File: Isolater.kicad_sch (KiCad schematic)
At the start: 15 parts, among them J29 Norcomp 172-009-243R021, J30 Pin Socket 0.1" 01x04, J32 Pin Socket 0.1" 01x04, U1 UCC12040DVE, U2 L7805CDT, U3 ISO1050DUB

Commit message: fix drc/erc errors
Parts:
- U1: footprint SO_0DVER_TEX -> footprints:SO_0DVER_TEX
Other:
- note removed: "TODO: verify dsub footprint"
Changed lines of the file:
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@@
     (stroke (width 0) (type default))
-  )
-  (text "TODO: verify dsub footprint\n" (at 15.24 24.13 0)
-    (effects (font (size 3 3) (thickness 0.8) bold (color 255 4 17 1)) (justify left bottom))
   )
   (text "Place close to connector" (at 154.94 95.25 0)
@@
       (effects (font (size 1.524 1.524)))
     )
-    (property "Footprint" "SO_0DVER_TEX" (at 207.01 40.64 0)
+    (property "Footprint" "footprints:SO_0DVER_TEX" (at 207.01 40.64 0)
       (effects (font (size 1.27 1.27) italic) hide)
     )

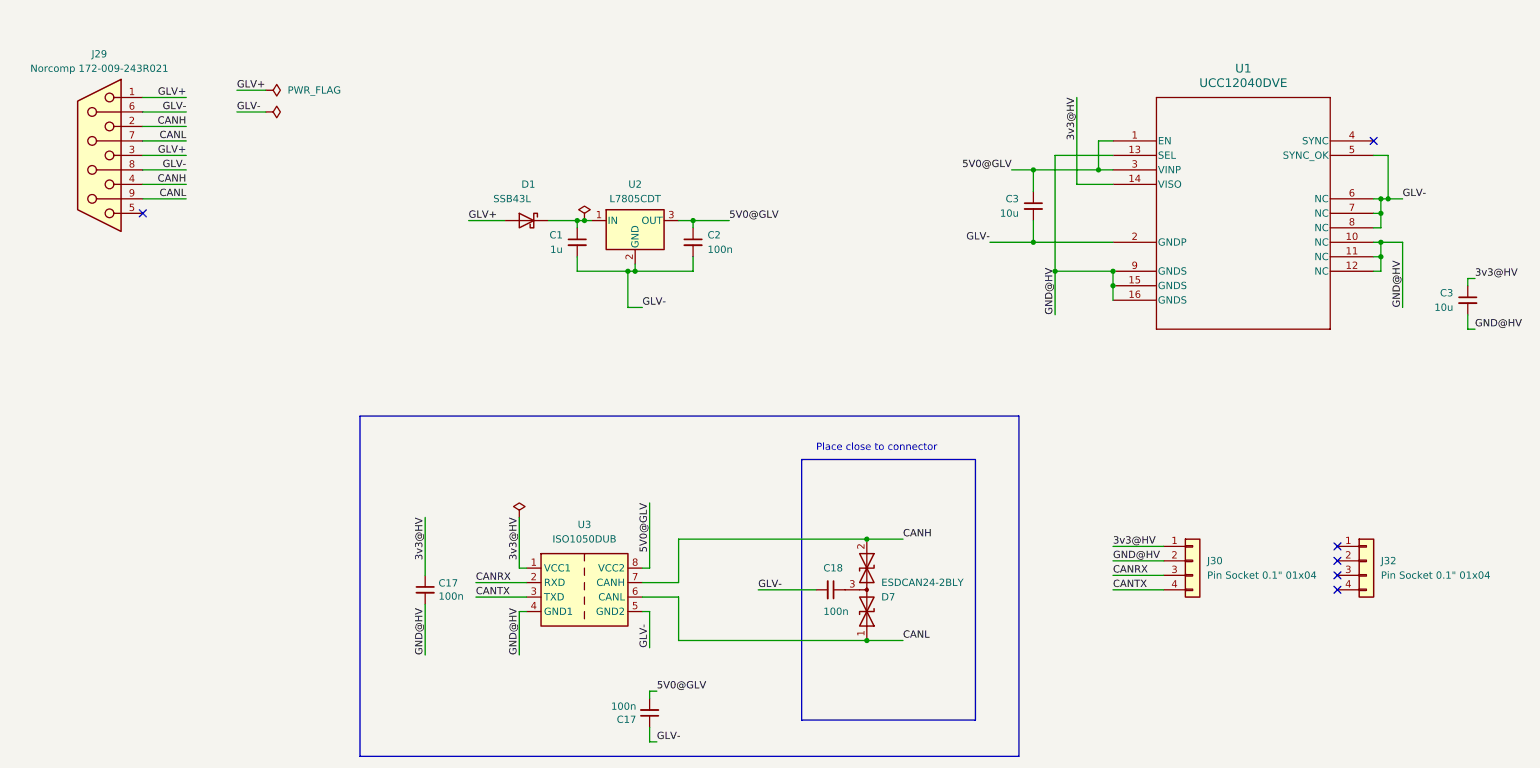
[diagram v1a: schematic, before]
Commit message: update firmware to do calibration and work with orion BMS
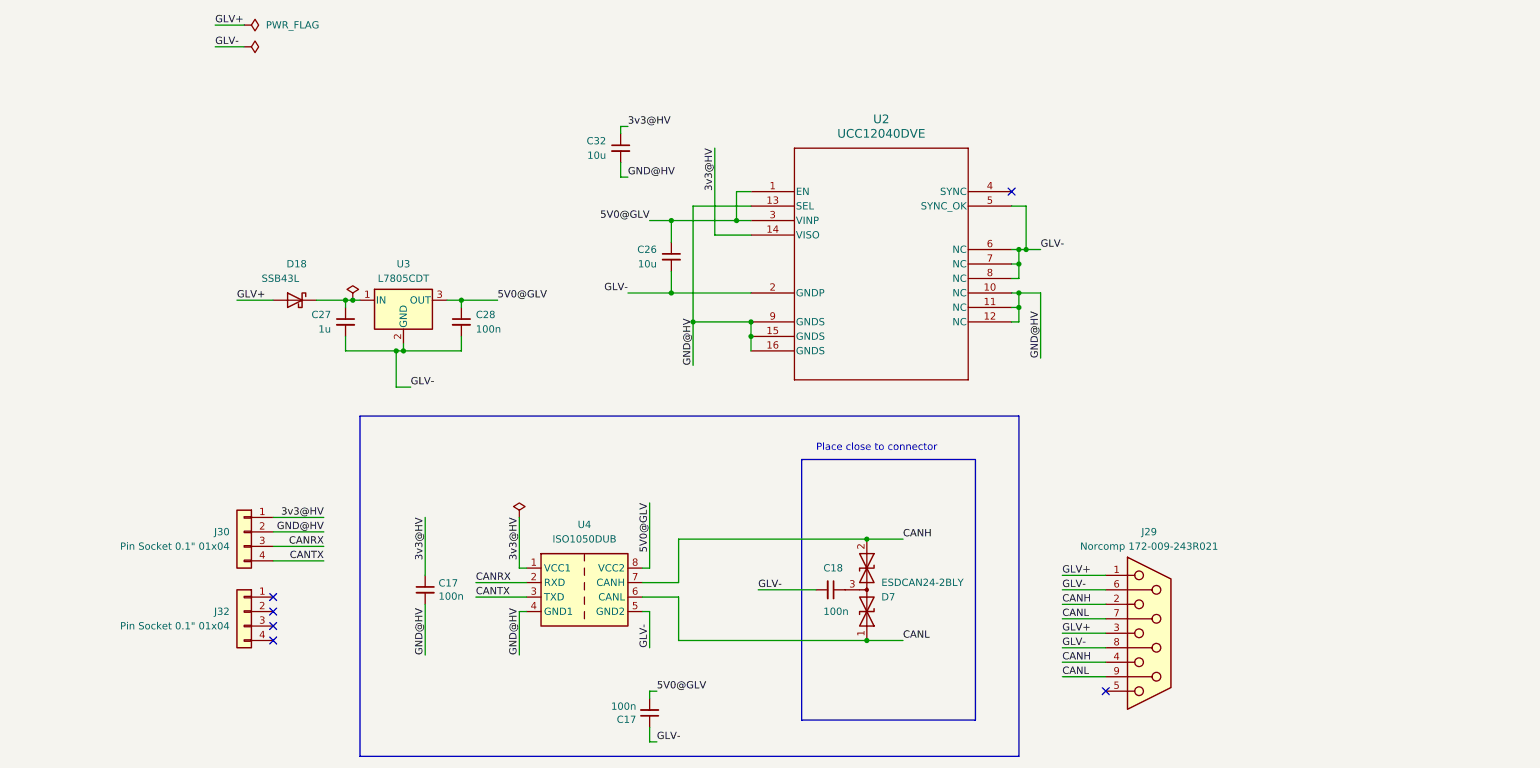
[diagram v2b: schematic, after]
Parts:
- renumbered C3 to C26, C1 to C27, C2 to C28, C3 to C32, D1 to D18, U1 to U2, U2 to U3, U3 to U4
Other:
- moved on the sheet: C26, C27, C28, C32, D18, J29, J30, J32, U2, U3
